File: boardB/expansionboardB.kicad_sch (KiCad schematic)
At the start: 42 parts, among them J1 USB_C_Receptacle, J3 HDMI_A, SW3 ESPRESET, SW4 ESPPROG, U1 ESP32-S3-WROOM-1, U2 GPIO_U2, U4 GPIO_U4, U5 SII1136CTU, U7 MAX20022ATIA+T

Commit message: Updates to new board
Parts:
- removed AU1: SJ-3523-SMT-TR, SJ-3523-SMT-TR:CUI_SJ-3523-SMT-TR, symbol SJ-3523-SMT-TR:SJ-3523-SMT-TR
- removed C8, C9: 1uf, Capacitor_SMD:C_0603_1608Metric_Pad1.08x0.95mm_HandSolder, symbol Device:C
- removed R7, R8: 33Ohm, Resistor_SMD:R_0603_1608Metric_Pad0.98x0.95mm_HandSolder, symbol Device:R
- added C13: 2.2uf, Capacitor_SMD:C_0603_1608Metric_Pad1.08x0.95mm_HandSolder, symbol Device:C
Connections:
- net VOUT_1 is gone; now on net REG3V3: L1.1
- net VOUT_2 is gone; now on net REG1V2: L2.1
- net VOUT_3 is gone; now on net REG1V0: L3.2
- net 5V: now also U7.15 (PV3), C13.1
- net AU_MCLK: now also U5.36 (MCLK)
- net AU_SCLK: now also U5.35 (SCK)
- net GND: now also C13.2; no longer U7.18 (PGND4)
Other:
- note removed: "Audio Out"
- moved on the sheet: C2, C3

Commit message: Updated new board
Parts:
- removed C11: 10uf, Capacitor_SMD:C_0603_1608Metric_Pad1.08x0.95mm_HandSolder, symbol Device:C
- removed C13: 2.2uf, Capacitor_SMD:C_0603_1608Metric_Pad1.08x0.95mm_HandSolder, symbol Device:C
- removed L3: 1.5uH, Inductor_SMD:L_0805_2012Metric, symbol Device:L
- added FB2, FB3: 1k@100MHz, Resistor_SMD:R_0805_2012Metric_Pad1.20x1.40mm_HandSolder, symbol graphics-card-rev-2-rescue:Ferrite_Bead-Device
- added R13, R8: 2K0, Resistor_SMD:R_0603_1608Metric_Pad0.98x0.95mm_HandSolder, symbol Device:R
- added R14: 27K0, Resistor_SMD:R_0603_1608Metric_Pad0.98x0.95mm_HandSolder, symbol Device:R
- added R7: 4K7, Resistor_SMD:R_0603_1608Metric_Pad0.98x0.95mm_HandSolder, symbol Device:R
- added t1V2: 1V2_TEST, TestPoint:TestPoint_Pad_D1.5mm, symbol Connector:TestPoint
- added t3V3: 3V3_TEST, TestPoint:TestPoint_Pad_D1.5mm, symbol Connector:TestPoint
- added tSCL1: SCL_TEST, TestPoint:TestPoint_Pad_D1.5mm, symbol Connector:TestPoint
- added tSDA1: SDA_TEST, TestPoint:TestPoint_Pad_D1.5mm, symbol Connector:TestPoint
- R1, R10: value 23K -> 23K0
- R11, R12: value 10K -> 10K0
- R2: value 10KOhm -> 10K0
- R3, R4, R5, R6: value 33Ohm -> 33
- R9: value 510Ohm -> 4K06
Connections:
- net AVINT is gone; now on net VID_INT: U5.46 (INT)
- net VDAT0 is gone; now on net VB1: U4.48 (Pin_48)
- net VDAT1 is gone; now on net VB0: U4.47 (Pin_47)
- net VDAT10 is gone; now on net VG3: U4.38 (Pin_38)
- net VDAT11 is gone; now on net VG2: U4.37 (Pin_37)
- net VDAT2 is gone; now on net VB3: U4.46 (Pin_46)
- net VDAT3 is gone; now on net VB2: U4.45 (Pin_45)
- net VDAT4 is gone; now on net VB5: U4.44 (Pin_44)
- net VDAT5 is gone; now on net VB4: U4.43 (Pin_43)
- net VDAT6 is gone; now on net VB7: U4.42 (Pin_42)
- net VDAT7 is gone; now on net VB6: U4.41 (Pin_41)
- net VDAT8 is gone; now on net VG1: U4.40 (Pin_40)
- net VDAT9 is gone; now on net VG0: U4.39 (Pin_39)
- net 5V: now also R13.1, R8.1; no longer U7.15 (PV3)
- net AU_LRCLK: now also U4.54 (Pin_54), U5.34 (WS_DR0); no longer U4.21 (Pin_21)
- net AU_MCLK: now also U4.56 (Pin_56); no longer U4.23 (Pin_23)
- net AU_SCLK: now also U4.55 (Pin_55); no longer U4.19 (Pin_19)
- net AU_SDIN: now also U4.53 (Pin_53), U5.33 (SD0_DL0); no longer U4.17 (Pin_17)
- net GND: now also R9.2, U5.17 (D3), U5.18 (D2), U5.19 (D1), U5.2 (D15), U5.20 (D0), U5.27 (DL3), U5.28 (DR3), U5.29 (SPDIF_IN_DL2), U5.3 (D14), U5.30 (SD3_DR2), U5.31 (SD2_DL1), U5.32 (SD1_DR1), U5.4 (D13), U5.6 (D12), U5.86 (D27), U5.87 (D26), U5.89 (D25), U5.90 (D24), U7.13 (EN3), U7.18 (PGND4), R7.2; no longer CRD1.P1 (SHIELD), CRD1.P2 (SHIELD), CRD1.P3 (SHIELD), CRD1.P4 (SHIELD), J1.S1 (SHIELD), J3.SH
- net REG1V2: now also U5.56 (AVCC), U5.61 (AVCC__1), FB2.2, t1V2.1; no longer C6.1, L2.1, R10.1
- net REG3V3: now also FB3.2, R14.2, t3V3.1; no longer C1.1, L1.1, R1.1, R9.2
- net VCLK: now also U4.50 (Pin_50); no longer U4.49 (Pin_49)
- net VDE: now also U4.51 (Pin_51); no longer U4.50 (Pin_50)
- net VHSYNC: now also U4.52 (Pin_52); no longer U4.51 (Pin_51)
- net VVSYNC: now also U4.49 (Pin_49); no longer U4.52 (Pin_52)
- net VR6: now reaches U4.25 (Pin_25)
- net VR6: now also U5.79 (D34)
- net VR7: now reaches U4.26 (Pin_26)
- net VR7: now also U5.78 (D35)
- net VR4: now reaches U4.27 (Pin_27)
- net VR4: now also U5.81 (D32)
- net VR5: now reaches U4.28 (Pin_28)
- net VR5: now also U5.80 (D33)
- net VR2: now reaches U4.29 (Pin_29)
- net VR2: now also U5.83 (D30)
- net VR3: now reaches U4.30 (Pin_30)
- net VR3: now also U5.82 (D31)
- net VR0: now reaches U4.31 (Pin_31)
- net VR0: now also U5.85 (D28)
- net VR1: now reaches U4.32 (Pin_32)
- net VR1: now also U5.84 (D29)
- net VG6: now reaches U4.33 (Pin_33)
- net VG6: now also U5.93 (D22)
- net VG7: now reaches U4.34 (Pin_34)
- net VG7: now also U5.92 (D23)
- net VG4: now reaches U4.35 (Pin_35)
- net VG4: now also U5.95 (D20)
- net VG5: now reaches U4.36 (Pin_36)
- net VG5: now also U5.94 (D21)
- net VID_SCL: now reaches U4.57 (Pin_57)
- net VID_SCL: now also U5.45 (CSCL)
- net VID_SDA: now reaches U4.58 (Pin_58)
- net VID_SDA: now also U5.44 (CSDA)
- net VID_INT: now reaches U4.59 (Pin_59)
- net VID_RESETN: now reaches U4.60 (Pin_60)
- net VID_RESETN: now also U5.47 (~{RESET})
- net VB4: now reaches U5.10 (D8)
- net VB3: now reaches U5.11 (D7)
- net VB2: now reaches U5.13 (D6)
- net VB1: now reaches U5.14 (D5)
- net VB0: now reaches U5.15 (D4)
- net D_CEC: now reaches U5.40 (CEC_A)
- net D_CEC: now also J3.13 (CEC), R14.1
- net D_SDA: now reaches U5.41 (DSDA)
- net D_SDA: now also J3.16 (SDA), R8.2, tSDA1.1
- net D_SCL: now reaches U5.42 (DSCL)
- net D_SCL: now also J3.15 (SCL), R13.2, tSCL1.1
- net at U5.43 (CI2CA): now also R7.1
- net VB7: now reaches U5.7 (D11)
- net D_HPD: now reaches U5.76 (HPD)
- net D_HPD: now also J3.19 (HPD)
- net VB6: now reaches U5.8 (D10)
- net VB5: now reaches U5.9 (D9)
- net VG3: now reaches U5.96 (D19)
- net VG2: now reaches U5.97 (D18)
- net VG1: now reaches U5.98 (D17)
- net VG0: now reaches U5.99 (D16)
- net PG_2: no longer names the net of U7.10 (PG2)
- net PG_2: no longer U7.13 (EN3)
- net REG1V0: no longer names the net of U7.14 (OUTS3)
- new net SHLD: CRD1.P1 (SHIELD), CRD1.P2 (SHIELD), CRD1.P3 (SHIELD), CRD1.P4 (SHIELD), J1.S1 (SHIELD), J3.SH
- new net VOUT_1: C1.1, FB3.1, L1.1, R1.1
- new net VOUT_2: C6.1, FB2.1, L2.1, R10.1
- no-connect marks 2 -> 0
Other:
- note added: "24 bit connection 8bpp RGB or YCbCr"
- note added: "5K6 for no internal termination (<165MHz) 4K02 for internal termination"
- note added: "640x480 (480p) ITU-R BT.601 Y = 0.299R′ + 0.587G′ + 0.114B′ Cb = –0.172R′ – 0.339G′ + 0.511B′ + 128 Cr = 0.511R′ – 0.428G′ – 0.083B′ + 128"
- note added: "BLUE"
- note added: "Blue or Cb0"
- note added: "CI2CA 0 1 ------------------------ Config Regs 0x7A 0x7E TPI 0x72 0x76 CPI 0xC0 0xC4"
- note added: "Configuration I2C"
- note added: "ESP32 Host Interface"
- note added: "GREEN"
- note added: "Green or Y0"
- note added: "Power Regulator (3V3, 1V2, 1V0)"
- note added: "RED"
- note added: "Red or Cr0"
- note added: "Use FPGA internal pullup or 4.7KOhm resistors tied to IOVCC"
- note removed: "Power Regulator (3V3, 1V2)"
- note removed: "Shield"
- note removed: "USB Host"
- moved on the sheet: C1, C10, C12, C2, C3, C4, C5, C6, C7, J1, J3, L1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

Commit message: Updates to new board
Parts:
- added E1: SparkGap, Diode_SMD:D_0201_0603Metric, symbol Device:SparkGap
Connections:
- net GND: now also E1.2
- net SHLD: now also E1.1
- net GPI: no longer names the net of U4.14 (Pin_14)
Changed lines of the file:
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@@
 	(wire
 		(pts
-			(xy 166.37 41.91) (xy 165.1 41.91)
-		)
-		(stroke
-			(width 0)
-			(type default)
-		)
-	)
-	(wire
-		(pts
 			(xy 261.62 246.38) (xy 271.78 246.38)
 		)
@@
 	(wire
 		(pts
+			(xy 257.81 64.77) (xy 262.89 64.77)
+		)
+		(stroke
+			(width 0)
+			(type default)
+		)
+	)
+	(wire
+		(pts
 			(xy 267.97 119.38) (xy 271.78 119.38)
 		)
@@
 	(wire
 		(pts
+			(xy 278.13 64.77) (xy 273.05 64.77)
+		)
+		(stroke
+			(width 0)
+			(type default)
+		)
+	)
+	(wire
+		(pts
 			(xy 281.94 271.78) (xy 285.75 271.78)
 		)
@@
 		)
 	)
+	(global_label "SHLD"
+		(shape input)
+		(at 257.81 64.77 180)
+		(fields_autoplaced yes)
+		(effects
+			(font
+				(size 1.27 1.27)
+			)
+			(justify right)
+		)
+		(property "Intersheetrefs" "${INTERSHEET_REFS}"
+			(at 249.9867 64.77 0)
+			(effects
+				(font
+					(size 1.27 1.27)
+				)
+				(justify right)
+				(hide yes)
+			)
+		)
+	)
 	(global_label "VR7"
 		(shape output)
@@
 		)
 	)
+	(global_label "GND"
+		(shape input)
+		(at 278.13 64.77 0)
+		(fields_autoplaced yes)
+		(effects
+			(font
+				(size 1.27 1.27)
+			)
+			(justify left)
+		)
+		(property "Intersheetrefs" "${INTERSHEET_REFS}"
+			(at 284.9857 64.77 0)
+			(effects
+				(font
+					(size 1.27 1.27)
+				)
+				(justify left)
+				(hide yes)
+			)
+		)
+	)
 	(global_label "VR6"
 		(shape output)
@@
 		)
 	)
-	(global_label "GPI"
-		(shape output)
-		(at 166.37 41.91 0)
-		(fields_autoplaced yes)
-		(effects
-			(font
-				(size 1.27 1.27)
-			)
-			(justify left)
-		)
-		(property "Intersheetrefs" "${INTERSHEET_REFS}"
-			(at 172.5 41.91 0)
-			(effects
-				(font
-					(size 1.27 1.27)
-				)
-				(justify left)
-				(hide yes)
-			)
-		)
-	)
 	(global_label "VVSYNC"
 		(shape input)
@@
 					(unit 1)
 				)
+			)
+		)
+	)
+	(symbol
+		(lib_id "Device:SparkGap")
+		(at 267.97 64.77 0)
+		(unit 1)
+		(exclude_from_sim no)
+		(in_bom yes)
+		(on_board yes)
+		(dnp no)
+		(fields_autoplaced yes)
+		(property "Reference" "E1"
+			(at 267.97 59.69 0)
+			(effects
+				(font
+					(size 1.27 1.27)
+				)
+			)
+		)
+		(property "Value" "SparkGap"
+			(at 267.97 62.23 0)
+			(effects
+				(font
+					(size 1.27 1.27)
+				)
+			)
+		)
+		(property "Footprint" "Diode_SMD:D_0201_0603Metric"
+			(at 267.97 66.548 0)
+			(effects
+				(font
+					(size 1.27 1.27)
+				)
+				(hide yes)
+			)
+		)
+		(property "Datasheet" "~"
+			(at 267.97 64.77 90)
+			(effects
+				(font
+					(size 1.27 1.27)
+				)
+				(hide yes)
+			)
+		)
+		(property "Description" "Spark gap"
+			(at 267.97 64.77 0)
+			(effects
+				(font
+					(size 1.27 1.27)
+				)
+				(hide yes)
+			)
+		)
+		(pin "1"
+		)
+		(pin "2"
+		)
+		(instances
+			(project ""
+				(path "/317f7f3e-4535-46d0-9a87-af1bea12706a"
+					(reference "E1")
+					(unit 1)
+				)

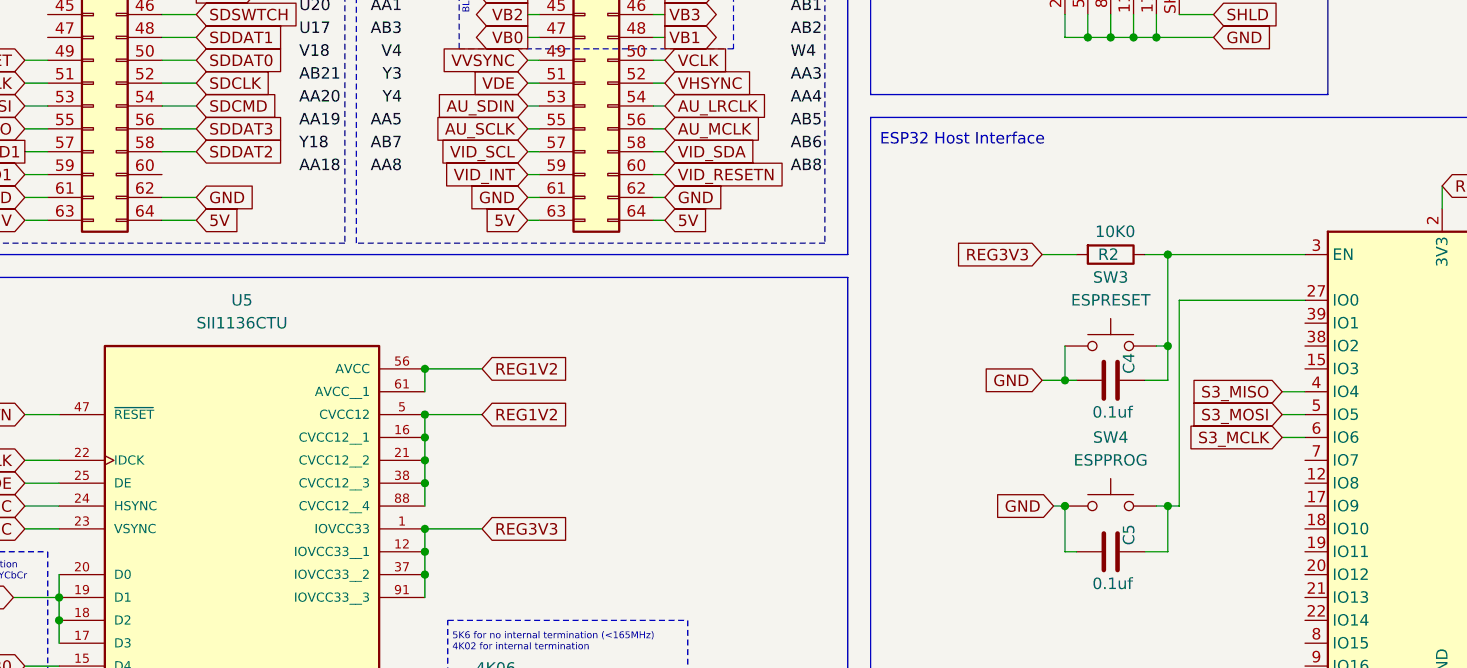
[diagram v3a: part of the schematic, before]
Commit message: Updated board and hardware to reset ESP32 from the FPGA
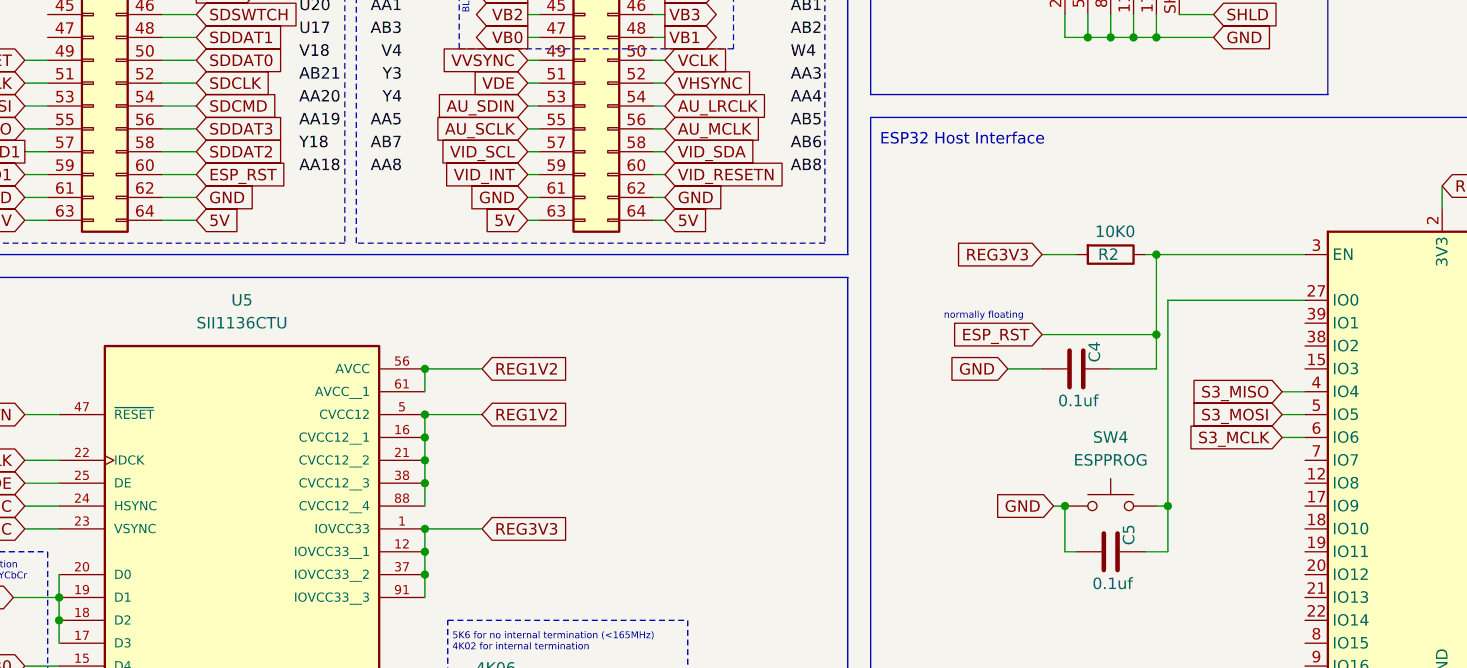
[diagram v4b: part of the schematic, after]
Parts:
- removed SW3: ESPRESET, Button_Switch_SMD:SW_Tactile_SPST_NO_Straight_CK_PTS636Sx25SMTRLFS, symbol Switch:SW_Push
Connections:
- net ESP_RST: now reaches C4.1, R2.1, U1.3 (EN)
- net ESP_RST: now also U2.60 (Pin_60)
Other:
- note added: "normally floating"
- moved on the sheet: C4
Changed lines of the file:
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@@
 	)
 	(junction
+		(at 220.98 118.11)
+		(diameter 0)
+		(color 0 0 0 0)
+	)
+	(junction
 		(at 279.4 236.22)
 		(diameter 0)
@@
 	)
 	(junction
-		(at 222.25 119.38)
-		(diameter 0)
-		(color 0 0 0 0)
-	)
-	(junction
 		(at 162.56 233.68)
 		(diameter 0)
@@
 	)
 	(junction
-		(at 222.25 109.22)
-		(diameter 0)
-		(color 0 0 0 0)
-	)
-	(junction
 		(at 173.99 233.68)
 		(diameter 0)
@@
 	)
 	(junction
+		(at 220.98 109.22)
+		(diameter 0)
+		(color 0 0 0 0)
+	)
+	(junction
 		(at 212.09 279.4)
 		(diameter 0)
@@
 	)
 	(junction
-		(at 210.82 123.19)
-		(diameter 0)
-		(color 0 0 0 0)
-	)
-	(junction
 		(at 99.06 180.34)
 		(diameter 0)
@@
 	(wire
 		(pts
-			(xy 208.28 123.19) (xy 210.82 123.19)
+			(xy 204.47 121.92) (xy 208.28 121.92)
 		)
 		(stroke
@@
 	(wire
 		(pts
-			(xy 222.25 119.38) (xy 222.25 123.19)
-		)
-		(stroke
-			(width 0)
-			(type default)
-		)
-	)
-	(wire
-		(pts
 			(xy 58.42 96.52) (xy 60.96 96.52)
 		)
@@
 	(wire
 		(pts
-			(xy 223.52 137.16) (xy 223.52 114.3)
+			(xy 222.25 137.16) (xy 222.25 114.3)
 		)
 		(stroke
@@
 	(wire
 		(pts
-			(xy 222.25 137.16) (xy 223.52 137.16)
-		)
-		(stroke
-			(width 0)
-			(type default)
-		)
-	)
-	(wire
-		(pts
 			(xy 166.37 92.71) (xy 165.1 92.71)
 		)
@@
 	(wire
 		(pts
-			(xy 210.82 119.38) (xy 210.82 123.19)
-		)
-		(stroke
-			(width 0)
-			(type default)
-		)
-	)
-	(wire
-		(pts
 			(xy 152.4 62.23) (xy 151.13 62.23)
 		)
@@
 	(wire
 		(pts
-			(xy 210.82 123.19) (xy 212.09 123.19)
-		)
-		(stroke
-			(width 0)
-			(type default)
-		)
-	)
-	(wire
-		(pts
 			(xy 212.09 262.89) (xy 212.09 266.7)
 		)
@@
 	(wire
 		(pts
-			(xy 222.25 109.22) (xy 237.49 109.22)
+			(xy 220.98 109.22) (xy 237.49 109.22)
 		)
 		(stroke
@@
 	(wire
 		(pts
-			(xy 219.71 109.22) (xy 222.25 109.22)
+			(xy 219.71 109.22) (xy 220.98 109.22)
 		)
 		(stroke
@@
 	(wire
 		(pts
+			(xy 208.28 118.11) (xy 220.98 118.11)
+		)
+		(stroke
+			(width 0)
+			(type default)
+		)
+	)
+	(wire
+		(pts
 			(xy 212.09 142.24) (xy 210.82 142.24)
 		)
@@
 	(wire
 		(pts
+			(xy 220.98 118.11) (xy 220.98 121.92)
+		)
+		(stroke
+			(width 0)
+			(type default)
+		)
+	)
+	(wire
+		(pts
 			(xy 139.7 139.7) (xy 139.7 142.24)
 		)
@@
 	(wire
 		(pts
+			(xy 114.3 100.33) (xy 110.49 100.33)
+		)
+		(stroke
+			(width 0)
+			(type default)
+		)
+	)
+	(wire
+		(pts
 			(xy 166.37 67.31) (xy 165.1 67.31)
 		)
@@
 	(wire
 		(pts
-			(xy 220.98 119.38) (xy 222.25 119.38)
-		)
-		(stroke
-			(width 0)
-			(type default)
-		)
-	)
-	(wire
-		(pts
 			(xy 152.4 95.25) (xy 151.13 95.25)
 		)
@@
 	(wire
 		(pts
-			(xy 223.52 114.3) (xy 237.49 114.3)
+			(xy 222.25 114.3) (xy 237.49 114.3)
 		)
 		(stroke
@@
 	(wire
 		(pts
-			(xy 219.71 123.19) (xy 222.25 123.19)
+			(xy 215.9 121.92) (xy 220.98 121.92)
 		)
 		(stroke
@@
 	(wire
 		(pts
-			(xy 222.25 109.22) (xy 222.25 119.38)
+			(xy 220.98 109.22) (xy 220.98 118.11)
 		)
 		(stroke
@@
 		)
 	)
+	(text "normally floating"
+		(exclude_from_sim no)
+		(at 197.358 116.586 0)
+		(effects
+			(font
+				(size 0.762 0.762)
+			)
+			(justify left bottom)
+		)
+	)
 	(text "3V3 -> R1=R2*2.3\nR1==23KOhm\nR2==10KOhm\nC1==15pF"
 		(exclude_from_sim no)
@@
 		)
 	)
+	(global_label "ESP_RST"
+		(shape input)
+		(at 114.3 100.33 0)
+		(fields_autoplaced yes)
+		(effects
+			(font
+				(size 1.27 1.27)
+			)
+			(justify left)
+		)
+		(property "Intersheetrefs" "${INTERSHEET_REFS}"
+			(at 125.3284 100.33 0)
+			(effects
+				(font
+					(size 1.27 1.27)
+				)
+				(justify left)
+				(hide yes)
+			)
+		)
+	)
 	(global_label "VG2"
 		(shape input)
@@
 		)
 	)
+	(global_label "ESP_RST"
+		(shape input)
+		(at 208.28 118.11 180)
+		(fields_autoplaced yes)
+		(effects
+			(font
+				(size 1.27 1.27)
+			)
+			(justify right)
+		)
+		(property "Intersheetrefs" "${INTERSHEET_REFS}"
+			(at 197.2516 118.11 0)
+			(effects
+				(font
+					(size 1.27 1.27)
+				)
+				(justify right)
+				(hide yes)
+			)
+		)
+	)
 	(global_label "VVSYNC"
 		(shape input)
@@
 	(global_label "GND"
 		(shape input)
-		(at 208.28 123.19 180)
+		(at 204.47 121.92 180)
 		(fields_autoplaced yes)
 		(effects
@@
 		)
 		(property "Intersheetrefs" "${INTERSHEET_REFS}"
-			(at 201.4243 123.19 0)
+			(at 197.6143 121.92 0)
 			(effects
 				(font
@@
 	(symbol
 		(lib_id "Device:C")
-		(at 215.9 123.19 270)
+		(at 212.09 121.92 270)
 		(unit 1)
 		(exclude_from_sim no)
@@
 		(dnp no)
 		(property "Reference" "C4"
-			(at 217.932 120.142 0)
+			(at 214.122 118.872 0)
 			(effects
 				(font
@@
 		)
 		(property "Value" "0.1uf"
-			(at 213.868 126.746 90)
+			(at 210.058 125.476 90)
 			(effects
 				(font
@@
 		)
 		(property "Footprint" "Capacitor_SMD:C_0603_1608Metric_Pad1.08x0.95mm_HandSolder"
-			(at 212.09 124.1552 0)
+			(at 208.28 122.8852 0)
 			(effects
 				(font
@@
 		)
 		(property "Datasheet" "~"
-			(at 215.9 123.19 0)
+			(at 212.09 121.92 0)
 			(effects
 				(font
@@
 		)
 		(property "Description" ""
-			(at 215.9 123.19 0)
+			(at 212.09 121.92 0)
 			(effects
 				(font
@@
 					(unit 1)
 				)
-			)
-		)
-	)
-	(symbol
-		(lib_id "Switch:SW_Push")
-		(at 215.9 119.38 0)
-		(unit 1)
-		(exclude_from_sim no)
-		(in_bom yes)
-		(on_board yes)
-		(dnp no)
-		(fields_autoplaced yes)
-		(property "Reference" "SW3"
-			(at 215.9 111.76 0)
-			(effects
-				(font
-					(size 1.27 1.27)
-				)
-			)
-		)
-		(property "Value" "ESPRESET"
-			(at 215.9 114.3 0)
-			(effects
-				(font
-					(size 1.27 1.27)
-				)
-			)
-		)
-		(property "Footprint" "Button_Switch_SMD:SW_Tactile_SPST_NO_Straight_CK_PTS636Sx25SMTRLFS"
-			(at 215.9 114.3 0)
-			(effects
-				(font
-					(size 1.27 1.27)
-				)
-				(hide yes)
-			)
-		)
-		(property "Datasheet" "~"
-			(at 215.9 114.3 0)
-			(effects
-				(font
-					(size 1.27 1.27)
-				)
-				(hide yes)
-			)
-		)
-		(property "Description" "Push button switch, generic, two pins"
-			(at 215.9 119.38 0)
-			(effects
-				(font
-					(size 1.27 1.27)
-				)
-				(hide yes)
-			)
-		)
-		(pin "1"
-		)
-		(pin "2"
-		)
-		(instances
-			(project "expansionboardB"
-				(path "/317f7f3e-4535-46d0-9a87-af1bea12706a"
-					(reference "SW3")
-					(unit 1)
-				)

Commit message: minor repairs to boot time
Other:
- note added: "ESD Protection"
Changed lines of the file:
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@@
+	)
+	(rectangle
+		(start 243.84 55.88)
+		(end 294.64 71.12)
+		(stroke
+			(width 0)
+			(type default)
+		)
+		(fill
+			(type none)
+		)
 	)
 	(rectangle
@@
 			)
 			(justify left bottom)
+		)
+	)
+	(text "ESD Protection"
+		(exclude_from_sim no)
+		(at 244.856 58.928 0)
+		(effects
+			(font
+				(size 1.27 1.27)
+			)
+			(justify left bottom)

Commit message: New board updates
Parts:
- added JTAG1: Conn_01x06_Pin, Connector_PinHeader_2.54mm:PinHeader_1x06_P2.54mm_Vertical, symbol Connector:Conn_01x06_Pin
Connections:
- net GND: now also JTAG1.2 (Pin_2)
- net REG3V3: now also JTAG1.1 (Pin_1)
- net IO10: now reaches U2.33 (Pin_33)
- net IO10: now also U1.18 (IO10)
- net IO11: now reaches U2.35 (Pin_35)
- net IO11: now also U1.19 (IO11)
- net IO12: now reaches U2.37 (Pin_37)
- net IO12: now also U1.20 (IO12)
- net IO13: now reaches U2.39 (Pin_39)
- net IO13: now also U1.21 (IO13)
- net IO22: now reaches U2.41 (Pin_41)
- net IO22: now also U1.22 (IO14)
- net IO21: now reaches U2.43 (Pin_43)
- net IO21: now also U1.23 (IO21)
- net IO47: now reaches U2.45 (Pin_45)
- net IO47: now also U1.24 (IO47)
- net IO48: now reaches U2.47 (Pin_47)
- net IO48: now also U1.25 (IO48)
- net TDO: now reaches U4.11 (Pin_11)
- net TDO: now also JTAG1.4 (Pin_4)
- net TCK: now reaches U4.13 (Pin_13)
- net TCK: now also JTAG1.3 (Pin_3)
- net TMS: now reaches U4.7 (Pin_7)
- net TMS: now also JTAG1.6 (Pin_6)
- net TDI: now reaches U4.9 (Pin_9)
- net TDI: now also JTAG1.5 (Pin_5)
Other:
- note added: "JTAG"
